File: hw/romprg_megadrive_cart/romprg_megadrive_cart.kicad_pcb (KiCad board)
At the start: 2 copper layers, 92.1 x 53.3 mm, 2 parts, among them CON1 cartridge_connector

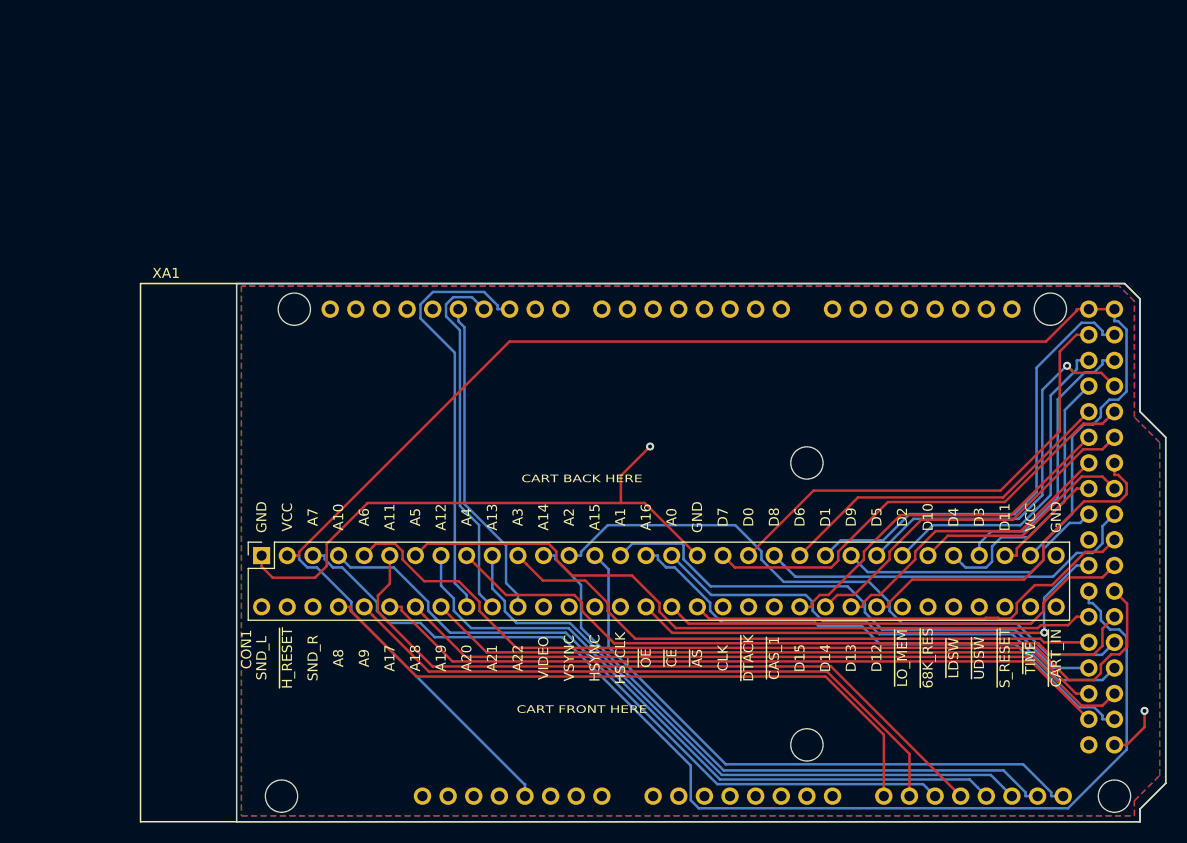
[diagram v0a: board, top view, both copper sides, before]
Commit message: more space for connector in case you get one with screw holes on sides
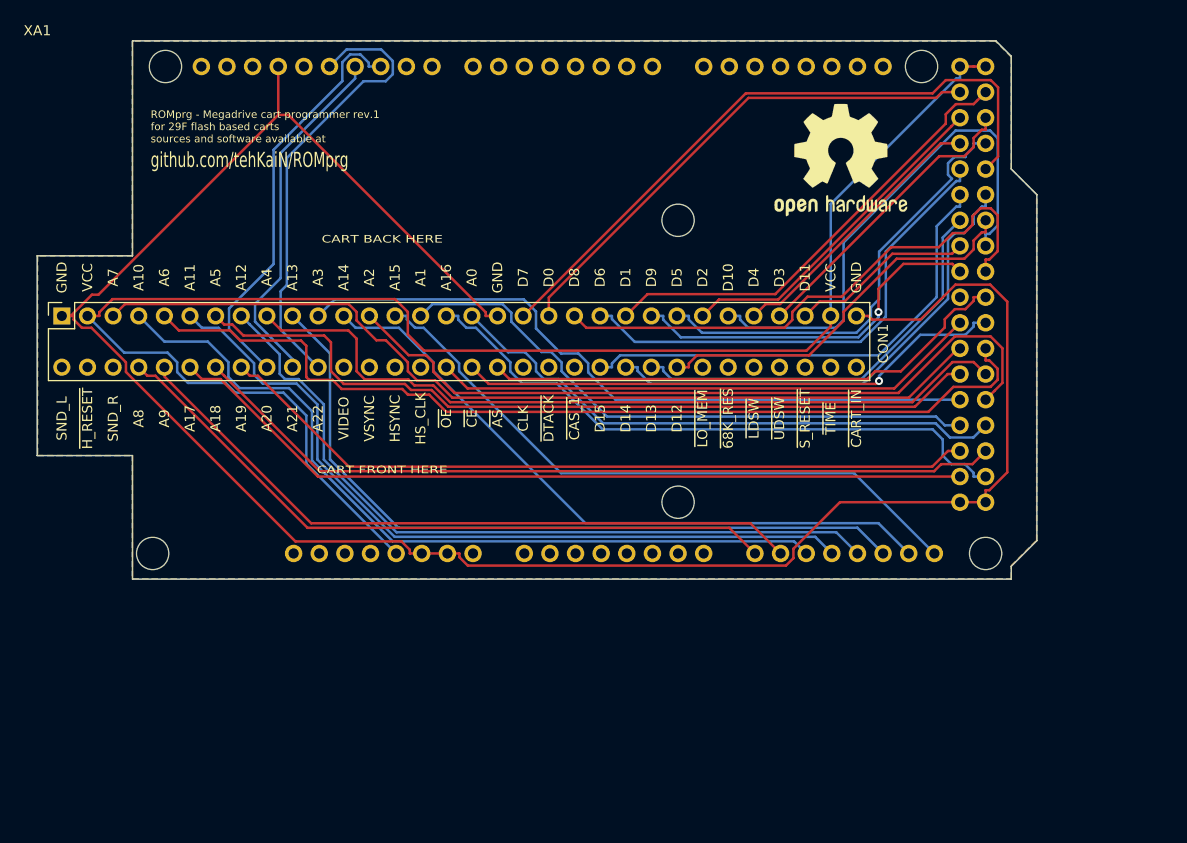
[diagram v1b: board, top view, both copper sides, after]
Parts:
- added REF**: OSHW-Logo2_14.6x12mm_SilkScreen, Symbol:OSHW-Logo2_14.6x12mm_SilkScreen, F.Cu at (129.9, 114.0)
- XA1: footprint romprg:Arduino_Mega2560_Shield_no_icsp -> romprg:Arduino_Mega2560_Shield_no_border
- moved CON1 30.9 mm to (52.7, 132.0)
- moved XA1 27.2 mm to (47.7, 102.2)
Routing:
- net GND: track 63.4 -> 208.2 mm, vias 2 -> 0
- net PC2: track 22.2 -> 51.7 mm
- net PL7: track 114.2 -> 91.3 mm
- net PA7: track 46.2 -> 65.6 mm
- net PC0: track 38.1 -> 54.9 mm
- net PA6: track 34.5 -> 48.5 mm
- net PB6: track 31.9 -> 45.2 mm
- net PC6: track 36.1 -> 49.0 mm
- net PL2: track 62.3 -> 75.0 mm
- net PC7: track 36.3 -> 47.8 mm
- net PC5: track 30.1 -> 41.3 mm
- net PK5: track 63.9 -> 74.4 mm
- net PK2: track 69.5 -> 79.6 mm
- net PC1: track 27.2 -> 36.7 mm, vias 0 -> 1
- net PL3: track 60.6 -> 69.9 mm
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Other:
- board size 92.1 x 53.3 mm -> 99.1 x 53.3 mm
- board text added: "ROMprg - Megadrive cart programmer rev.1 for 29F flash based carts sources and software available at"
- board text added: "github.com/tehKaiN/ROMprg"
